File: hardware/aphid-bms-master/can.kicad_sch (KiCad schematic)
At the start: 7 parts, among them U2 TJA1042T-3, U3 TJA1042T-3

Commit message: Assigned some footprints
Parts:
- L1, L2: footprint (none) -> aphid:DLW43SH
- R1: footprint (none) -> Resistor_SMD:R_0805_2012Metric
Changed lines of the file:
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@@
 			)
 		)
-		(property "Footprint" ""
+		(property "Footprint" "aphid:DLW43SH"
 			(at 143.51 118.11 0)
 			(effects
@@
 			)
 		)
-		(property "Footprint" ""
+		(property "Footprint" "Resistor_SMD:R_0805_2012Metric"
 			(at 157.48 124.968 90)
 			(effects
@@
 			)
 		)
-		(property "Footprint" ""
+		(property "Footprint" "aphid:DLW43SH"
 			(at 143.51 62.23 0)
 			(effects

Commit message: Worked on BMS master
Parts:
- added C22, C23, C24, C25: 100nF, Capacitor_SMD:C_0603_1608Metric, symbol Device:C
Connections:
- net +3.3V: now also C22.1, C23.1
- net +5V: now also U3.3 (VCC), C24.1, C25.1
- net GND: now also C22.2, C23.2, C24.2, C25.2
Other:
- company: (none) -> https://aphid-ev.se
- title: (none) -> Aphid BMS Master

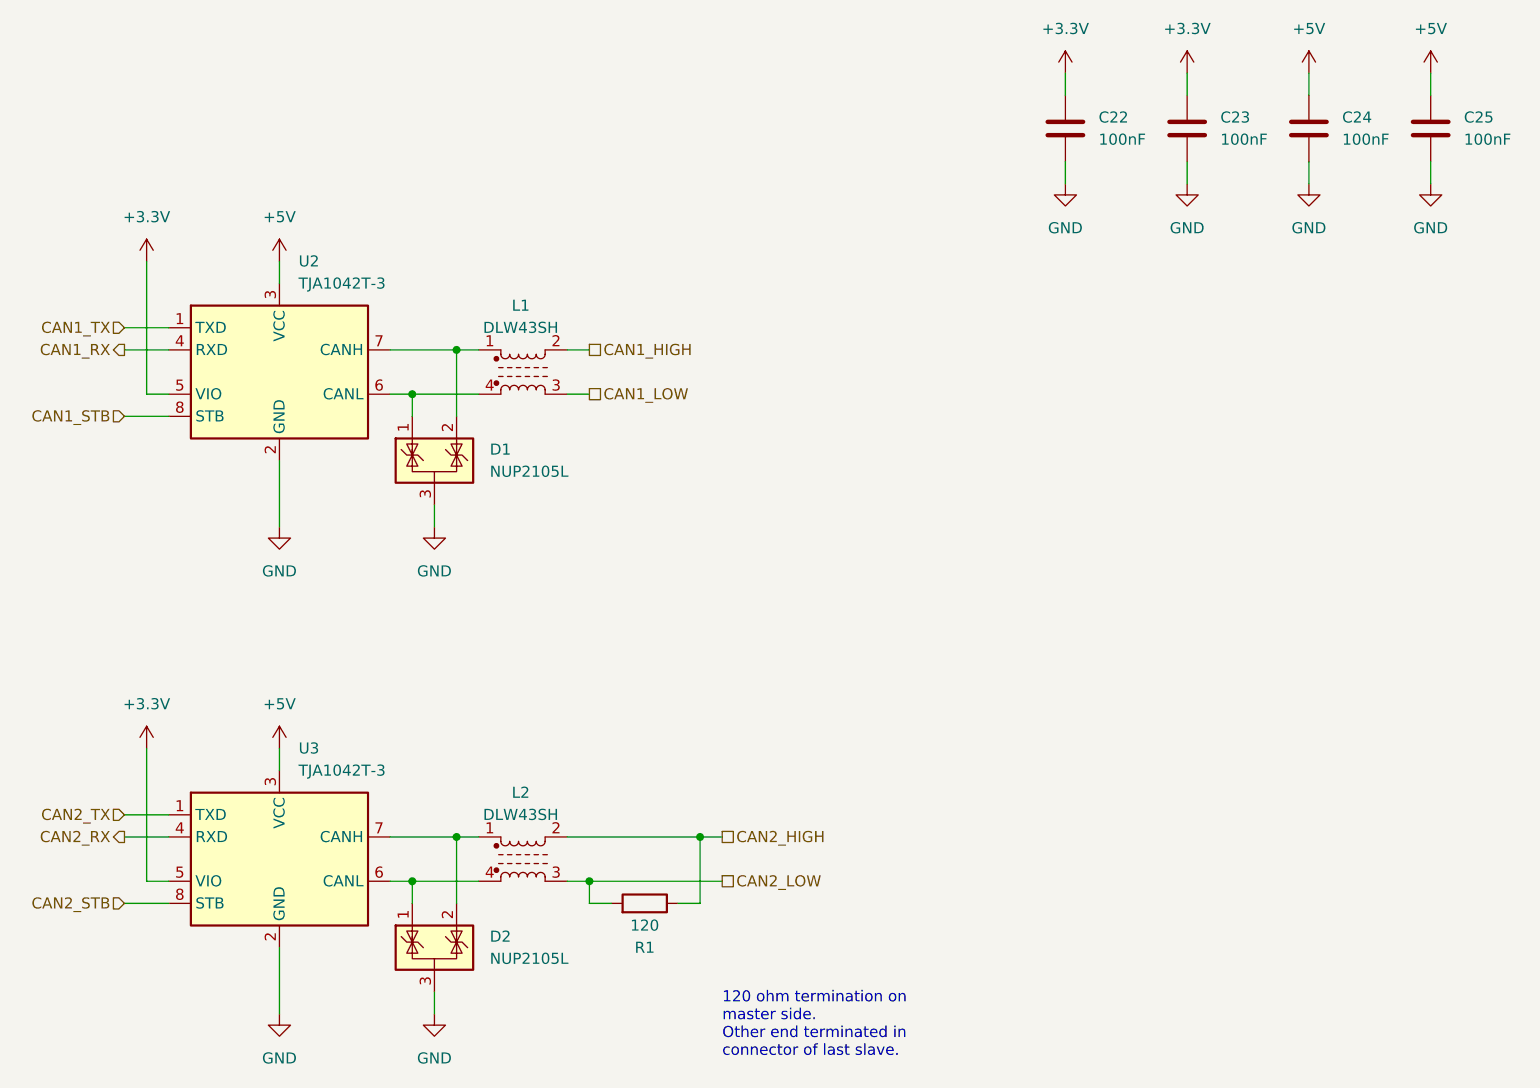
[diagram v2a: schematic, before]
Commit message: Changed BMS Master to use MAX17851 instead of isolated CAN
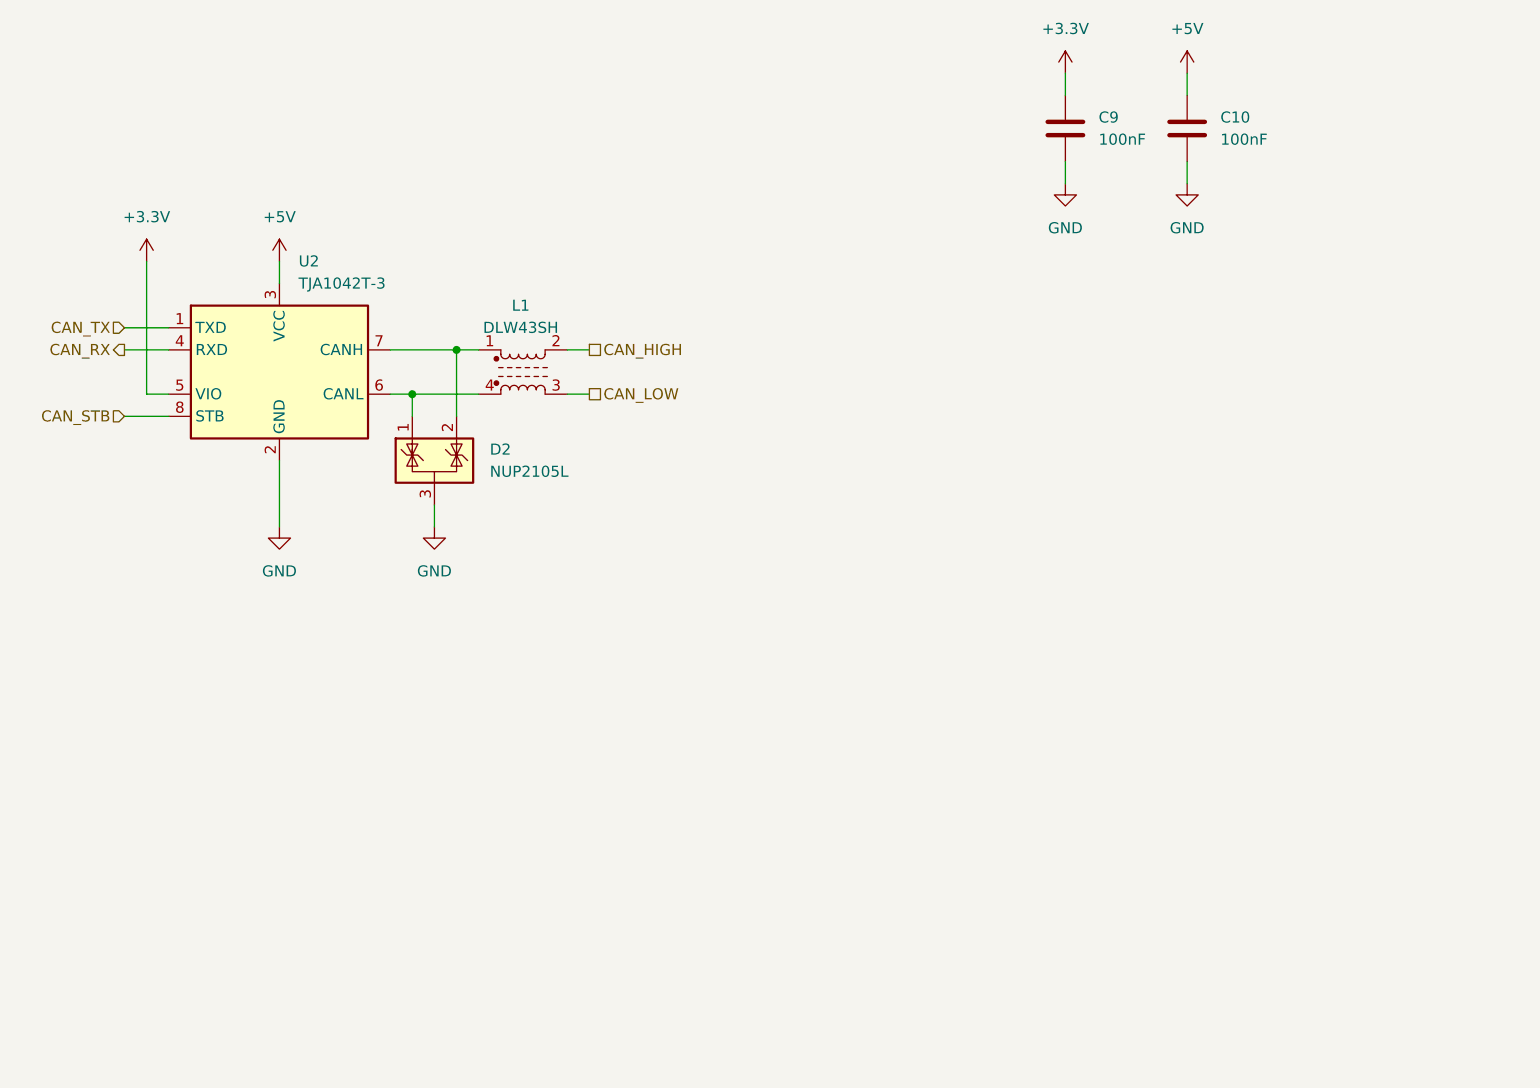
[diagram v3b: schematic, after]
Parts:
- removed C23, C25: 100nF, Capacitor_SMD:C_0603_1608Metric, symbol Device:C
- removed D2: NUP2105L, Package_TO_SOT_SMD:SOT-23, symbol Power_Protection:NUP2105L
- removed L2: DLW43SH, aphid:DLW43SH, symbol Device:L_Ferrite_Coupled_1243
- removed R1: 120, Resistor_SMD:R_0805_2012Metric, symbol Device:R
- removed U3: TJA1042T-3, Package_SO:SOIC-8_3.9x4.9mm_P1.27mm, symbol Interface_CAN_LIN:TJA1042T-3
- renumbered C24 to C10, C22 to C9, D1 to D2
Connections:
- net CAN1_HIGH renamed CAN_HIGH
- net CAN1_LOW renamed CAN_LOW
- net CAN1_RX renamed CAN_RX
- net CAN1_STB renamed CAN_STB
- net CAN1_TX renamed CAN_TX
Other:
- note removed: "120 ohm termination on master side. Other end terminated in connector of last slave."
- moved on the sheet: C10

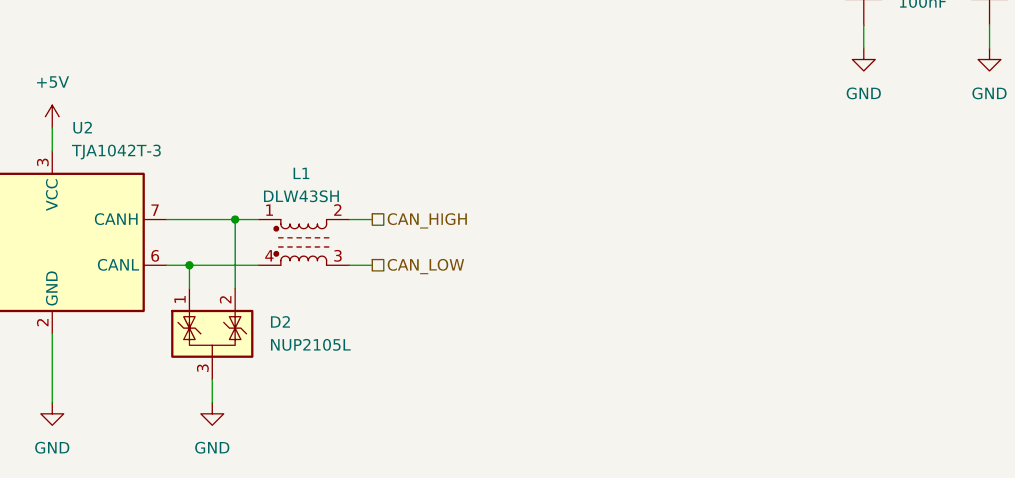
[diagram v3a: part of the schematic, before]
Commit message: Harmonized VC and BMS components
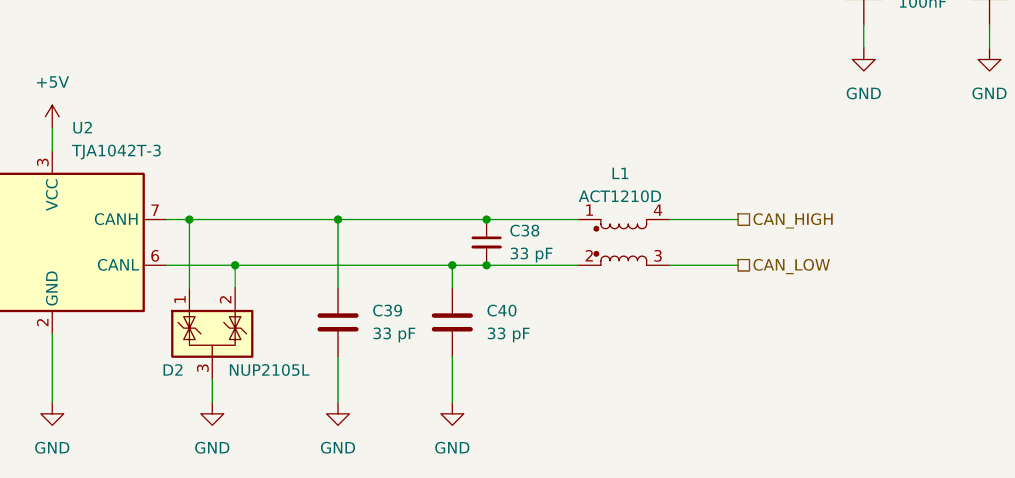
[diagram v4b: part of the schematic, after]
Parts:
- removed L1: DLW43SH, aphid:DLW43SH, symbol Device:L_Ferrite_Coupled_1243
- added C38: 33 pF, Capacitor_SMD:C_0603_1608Metric, symbol Device:C_Small
- added C39, C40: 33 pF, Capacitor_SMD:C_0603_1608Metric, symbol Device:C
- added L1: ACT1210D, aphid:ACT1210D, symbol Device:L_Coupled_1423
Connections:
- net CAN_HIGH: now also L1.4
- net CAN_LOW: now also L1.3
- net GND: now also C39.2, C40.2
- net at D2.1 (K): now also U2.7 (CANH), C38.1, C39.1, L1.1; no longer U2.6 (CANL)
- net at D2.2 (K): now also U2.6 (CANL), C38.2, C40.1, L1.2; no longer U2.7 (CANH)
